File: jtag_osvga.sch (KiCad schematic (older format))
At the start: 3 parts

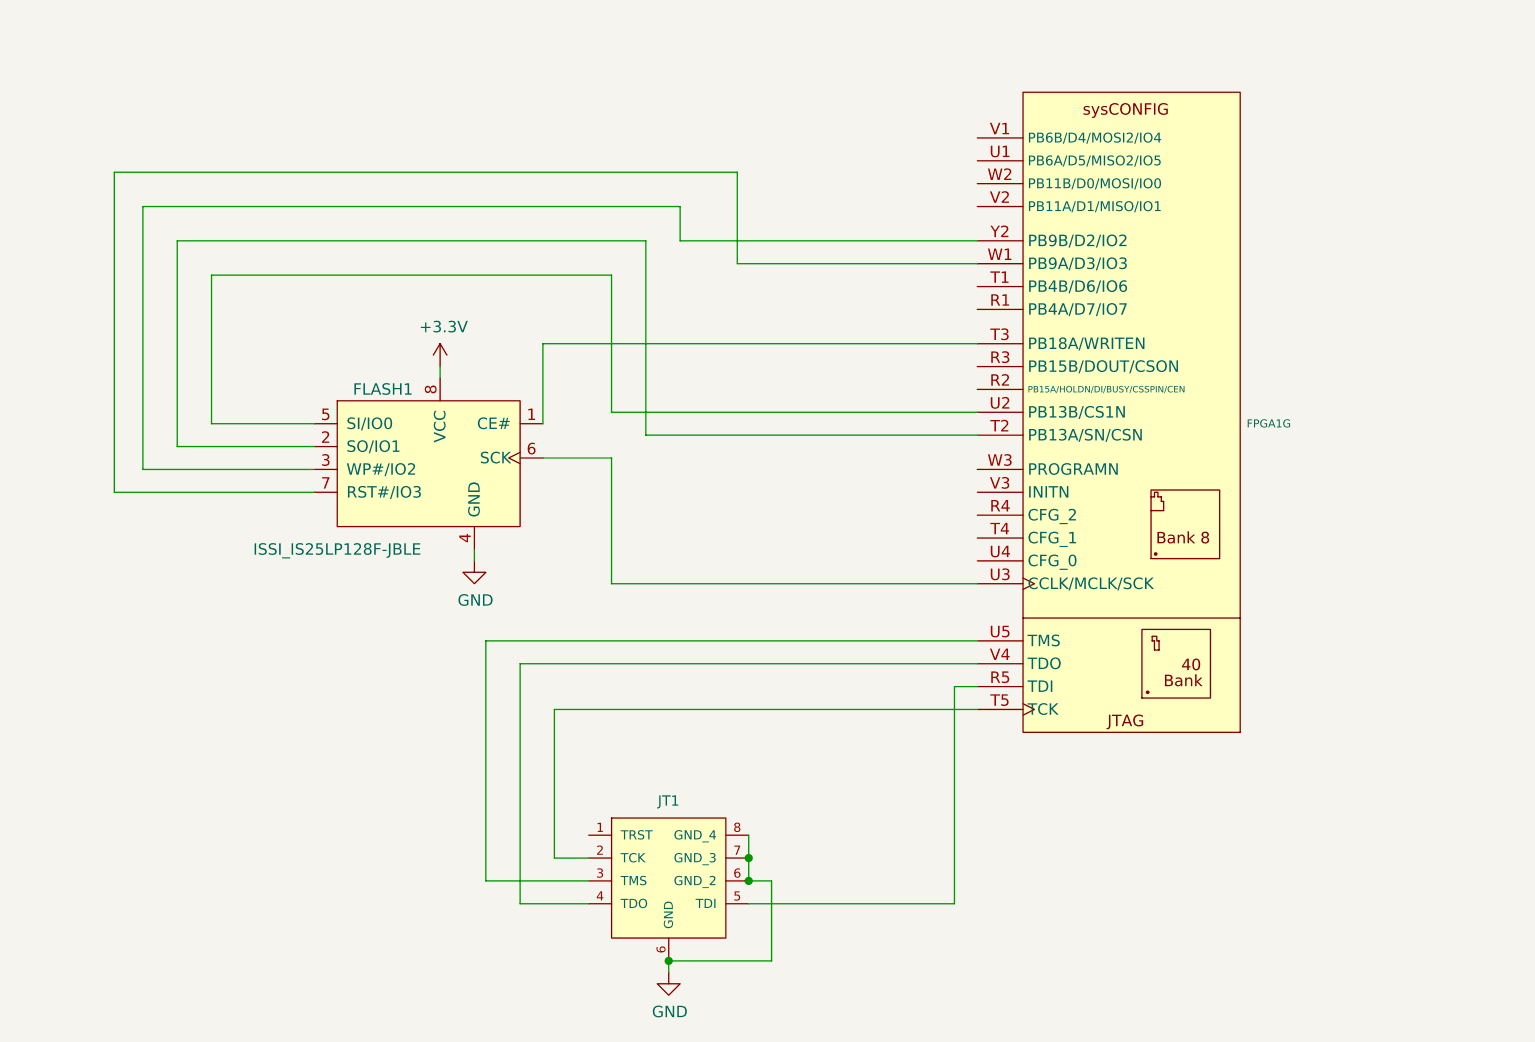
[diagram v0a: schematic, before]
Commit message: Add files via upload
Added Pull-up and pull-down resistors for JTAG and sysConfig connections.
Added pinheaders for FPGA-Configuration. (replacing edge-connector)
Combined the DVI+VGA and USB-C hierarchical sheets into one.
Assigned a dedicated sheet for the DAC.
Added 75 Ohm terminal-resistors to output of DAC.
Placed filtering-capacitors for DAC VAA.
Connected VGA ID-bits and DVI DDC together.
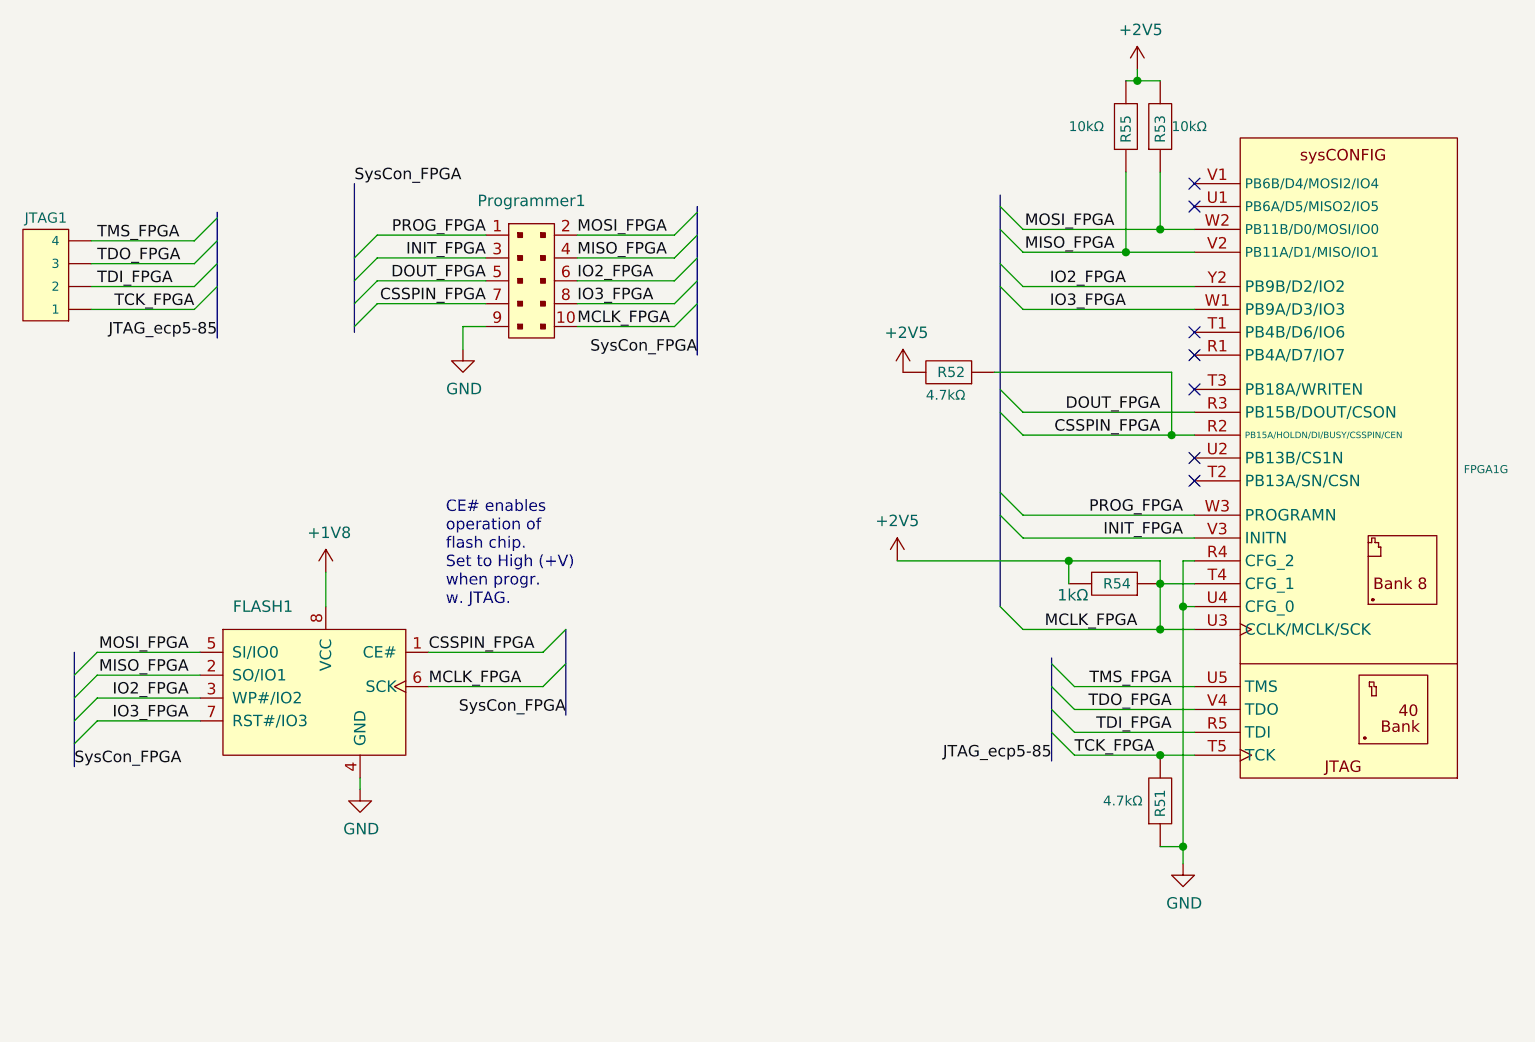
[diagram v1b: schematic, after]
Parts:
- removed FLASH1: ISSI_IS25LP128F-JBLE, Package_SO:SOIC-8_5.28x5.28mm_P1.27mm, symbol LRJ-parts:ISSI_IS25LP128F-JBLE
- removed JT1: CON-PCB-SLOT-0.05, Connector_PCBEdge:con-pcb-slot-CONN_SLOT, symbol svga-devboard-rescue:CON-PCB-SLOT-0.05-con-pcb-slot
- added FLASH1: ISSI_IS25WP128F-JBLE, Package_SO:SOIC-8_5.28x5.28mm_P1.27mm, symbol LRJ-parts:ISSI_IS25WP128F-JBLE
- added JTAG1: CONN_04JST-PTH, Connector_PinHeader_2.54mm:PinHeader_1x04_P2.54mm_Vertical, symbol SparkFun-Connectors:CONN_04JST-PTH
- added Programmer1: Wurth_WR-BHD_61201021721, Connector_PinHeader_2.54mm:WE_WR-BHD_RA_2x5_P2.54mm_Drill1.2mm, symbol LRJ-parts:Wurth_WR-BHD_61201021721
- added R51, R52: ERJ-8ENF4701V, Resistor_SMD:R_Panasonic_1206_3216Metric_ERJ8EN_HandSolder, symbol LRJ-parts:ERJ-8ENF4701V
- added R53, R55: ERJ-14YJ103U, Resistor_SMD:R_1210_3225Metric_Pad1.42x2.65mm_HandSolder, symbol LRJ-parts:ERJ-14YJ103U
- added R54: RC1210FR-071KL, Resistor_SMD:R_1210_3225Metric_Pad1.42x2.65mm_HandSolder, symbol LRJ-parts:RC1210FR-071KL
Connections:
- net GND: now also FPGA1.R4 (CFG_2), FPGA1.U4 (CFG_0), FLASH1.4 (GND), Programmer1.9, R51.1
- net TCK_FPGA: now reaches FPGA1.T5 (TCK)
- net TCK_FPGA: now also JTAG1.1, R51.2
- net TMS_FPGA: now reaches FPGA1.U5 (TMS)
- net TMS_FPGA: now also JTAG1.4
- net TDO_FPGA: now reaches FPGA1.V4 (TDO)
- net TDO_FPGA: now also JTAG1.3
- net TDI_FPGA: now reaches FPGA1.R5 (TDI)
- net TDI_FPGA: now also JTAG1.2
- net IO2_FPGA: now reaches FPGA1.Y2 (PB9B/D2/IO2)
- net IO2_FPGA: now also FLASH1.3 (WP#/IO2), Programmer1.6
- net +2V5: now reaches FPGA1.U3 (CCLK/MCLK/SCK)
- net +2V5: now also FPGA1.T4 (CFG_1), FLASH1.6 (SCK), Programmer1.10, R52.2, R53.2, R54.1, R54.2, R55.2
- net IO3_FPGA: now reaches FPGA1.W1 (PB9A/D3/IO3)
- net IO3_FPGA: now also FLASH1.7 (RST#/IO3), Programmer1.8
- net CSSPIN_FPGA: now reaches FPGA1.R2 (PB15A/HOLDN/DI/BUSY/CSSPIN/CEN)
- net CSSPIN_FPGA: now also FLASH1.1 (CE#), Programmer1.7, R52.1
- net DOUT_FPGA: now reaches FPGA1.R3 (PB15B/DOUT/CSON)
- net DOUT_FPGA: now also Programmer1.5
- net MISO_FPGA: now reaches FPGA1.V2 (PB11A/D1/MISO/IO1)
- net MISO_FPGA: now also FLASH1.2 (SO/IO1), Programmer1.4, R55.1
- net INIT_FPGA: now reaches FPGA1.V3 (INITN)
- net INIT_FPGA: now also Programmer1.3
- net MOSI_FPGA: now reaches FPGA1.W2 (PB11B/D0/MOSI/IO0)
- net MOSI_FPGA: now also FLASH1.5 (SI/IO0), Programmer1.2, R53.1
- net PROG_FPGA: now reaches FPGA1.W3 (PROGRAMN)
- net PROG_FPGA: now also Programmer1.1
- new net +1V8: FLASH1.8 (VCC)
- no-connect marks 0 -> 7
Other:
- note added: "CE# enables \noperation of \nflash chip.\nSet to High (+V) \nwhen progr.\nw. JTAG."
- moved on the sheet: FPGA1G

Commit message: Add files via upload
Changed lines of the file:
@@
 L power:+1V8 #PWR0151
 U 1 1 5F7BE59A
-P 4125 3800
-F 0 "#PWR0151" H 4125 3650 50  0001 C CNN
-F 1 "+1V8" H 4140 3973 50  0000 C CNN
-F 2 "" H 4125 3800 50  0001 C CNN
-F 3 "" H 4125 3800 50  0001 C CNN
-	1    4125 3800
-	1    0    0    -1
-$EndComp
-Wire Wire Line
-	4125 3950 4125 3800
+P 4050 3875
+F 0 "#PWR0151" H 4050 3725 50  0001 C CNN
+F 1 "+1V8" H 4065 4048 50  0000 C CNN
+F 2 "" H 4050 3875 50  0001 C CNN
+F 3 "" H 4050 3875 50  0001 C CNN
+	1    4050 3875
+	1    0    0    -1
+$EndComp
 $Comp
 L LRJ-parts:Wurth_WR-BHD_61201021721 Programmer1
@@
 NoConn ~ 7925 2200
 NoConn ~ 7925 2100
+Wire Wire Line
+	4050 3875 4125 3875
+Wire Wire Line
+	4125 3875 4125 3950
 Wire Bus Line
 	5175 4050 5175 4425
